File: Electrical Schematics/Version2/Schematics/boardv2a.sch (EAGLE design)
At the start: 622 parts, among them IC1 MCP41HVX1ST, IC2 ADUM4160BRW, IC3 SE555D, IC5 74LVC1G04DBV, IC6 74LVC1G04DBV, IC7 4030D, K1 G5V-2, K2 CP1SA-12V, Q1 IRLML2060TRPBFBSS123LT1G, Q10 IRLML2060TRPBFBSS123LT1G, Q11 IRLML2060TRPBFBSS123LT1G, Q12 IRLML2060TRPBFBSS123LT1G, Q13 IRLML2060TRPBFBSS123LT1G, Q17 IRLML2060TRPBFBSS123LT1G, Q18 MOSFET-PCHANNEL, Q19 IRLML2060TRPBFBSS123LT1G, Q2 IRLML2060TRPBFBSS123LT1G, Q3 IRLML2060TRPBFBSS123LT1G, Q4 MOSFET-PCHANNEL, Q5 MOSFET-PCHANNEL, Q6 IRLML2060TRPBFBSS123LT1G, Q7 ASFL1, Q8 IRLML2060TRPBFBSS123LT1G, Q9 IRLML2060TRPBFBSS123LT1G, U1 CP2130-GM, U10 SN65HVDA100-Q1_D_8, U11 ADUM3442CRWZ, U12 ADUM3442CRWZ, U13 ADUM3442CRWZ, U14 ADUM3442CRWZ, U15 ADUM3442CRWZ, U16 ADUM3442CRWZ, U17 ADUM3442CRWZ, U18 LM1085_KTT_3, U19 ADUM3442CRWZ, U2 TMS570LS0432_PZ_100, U20 ADUM3442CRWZ, U3 LM1085_KTT_3, U4 LM1085_KTT_3, U5 LM1084_KTT_3, U6 TPS3514_D_14, U7 LM1085_KTT_3, U9 ADUM3442CRWZ, X4 5566-4

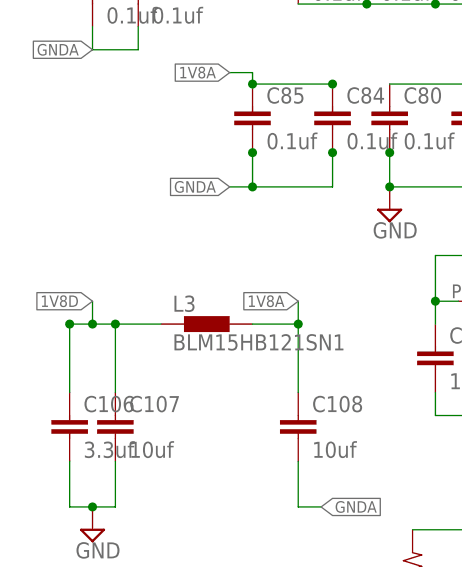
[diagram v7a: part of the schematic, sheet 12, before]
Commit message: routed lin ethernet and usb
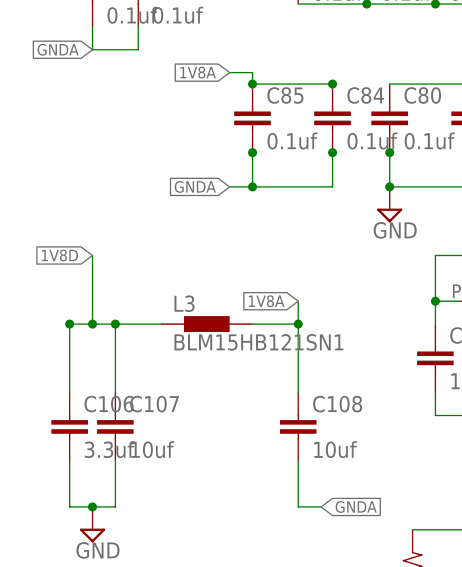
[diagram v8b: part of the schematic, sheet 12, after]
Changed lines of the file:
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@@
 <setting verticaltext="up"/>
 </settings>
-<grid distance="0.05" unitdist="inch" unit="inch" style="lines" multiple="1" display="no" altdistance="0.025" altunitdist="inch" altunit="inch"/>
+<grid distance="0.1" unitdist="inch" unit="inch" style="lines" multiple="1" display="no" altdistance="0.01" altunitdist="inch" altunit="inch"/>
 <layers>
-<layer number="1" name="Top" color="4" fill="1" visible="yes" active="no"/>
-<layer number="2" name="Route2" color="1" fill="3" visible="yes" active="no"/>
-<layer number="3" name="Route3" color="4" fill="3" visible="yes" active="no"/>
-<layer number="4" name="Route4" color="1" fill="4" visible="yes" active="no"/>
-<layer number="5" name="Route5" color="4" fill="4" visible="yes" active="no"/>
-<layer number="6" name="Route6" color="1" fill="8" visible="yes" active="no"/>
-<layer number="7" name="Route7" color="4" fill="8" visible="yes" active="no"/>
-<layer number="8" name="Route8" color="1" fill="2" visible="yes" active="no"/>
-<layer number="9" name="Route9" color="4" fill="2" visible="yes" active="no"/>
-<layer number="10" name="Route10" color="1" fill="7" visible="yes" active="no"/>
-<layer number="11" name="Route11" color="4" fill="7" visible="yes" active="no"/>
-<layer number="12" name="Route12" color="1" fill="5" visible="yes" active="no"/>
-<layer number="13" name="Route13" color="4" fill="5" visible="yes" active="no"/>
-<layer number="14" name="Route14" color="1" fill="6" visible="yes" active="no"/>
-<layer number="15" name="Route15" color="4" fill="6" visible="yes" active="no"/>
-<layer number="16" name="Bottom" color="1" fill="1" visible="yes" active="no"/>
-<layer number="17" name="Pads" color="2" fill="1" visible="yes" active="no"/>
-<layer number="18" name="Vias" color="2" fill="1" visible="yes" active="no"/>
-<layer number="19" name="Unrouted" color="6" fill="1" visible="yes" active="no"/>
-<layer number="20" name="Dimension" color="15" fill="1" visible="yes" active="no"/>
-<layer number="21" name="tPlace" color="7" fill="1" visible="yes" active="no"/>
-<layer number="22" name="bPlace" color="7" fill="1" visible="yes" active="no"/>
-<layer number="23" name="tOrigins" color="15" fill="1" visible="yes" active="no"/>
-<layer number="24" name="bOrigins" color="15" fill="1" visible="yes" active="no"/>
-<layer number="25" name="tNames" color="7" fill="1" visible="yes" active="no"/>
-<layer number="26" name="bNames" color="7" fill="1" visible="yes" active="no"/>
-<layer number="27" name="tValues" color="7" fill="1" visible="yes" active="no"/>
-<layer number="28" name="bValues" color="7" fill="1" visible="yes" active="no"/>
+<layer number="1" name="Top" color="4" fill="1" visible="no" active="no"/>
+<layer number="2" name="Route2" color="1" fill="3" visible="no" active="no"/>
+<layer number="3" name="Route3" color="4" fill="3" visible="no" active="no"/>
+<layer number="4" name="Route4" color="1" fill="4" visible="no" active="no"/>
+<layer number="5" name="Route5" color="4" fill="4" visible="no" active="no"/>
+<layer number="6" name="Route6" color="1" fill="8" visible="no" active="no"/>
+<layer number="7" name="Route7" color="4" fill="8" visible="no" active="no"/>
+<layer number="8" name="Route8" color="1" fill="2" visible="no" active="no"/>
+<layer number="9" name="Route9" color="4" fill="2" visible="no" active="no"/>
+<layer number="10" name="Route10" color="1" fill="7" visible="no" active="no"/>
+<layer number="11" name="Route11" color="4" fill="7" visible="no" active="no"/>
+<layer number="12" name="Route12" color="1" fill="5" visible="no" active="no"/>
+<layer number="13" name="Route13" color="4" fill="5" visible="no" active="no"/>
+<layer number="14" name="Route14" color="1" fill="6" visible="no" active="no"/>
+<layer number="15" name="Route15" color="4" fill="6" visible="no" active="no"/>
+<layer number="16" name="Bottom" color="1" fill="1" visible="no" active="no"/>
+<layer number="17" name="Pads" color="2" fill="1" visible="no" active="no"/>
+<layer number="18" name="Vias" color="2" fill="1" visible="no" active="no"/>
+<layer number="19" name="Unrouted" color="6" fill="1" visible="no" active="no"/>
+<layer number="20" name="Dimension" color="15" fill="1" visible="no" active="no"/>
+<layer number="21" name="tPlace" color="7" fill="1" visible="no" active="no"/>
+<layer number="22" name="bPlace" color="7" fill="1" visible="no" active="no"/>
+<layer number="23" name="tOrigins" color="15" fill="1" visible="no" active="no"/>
+<layer number="24" name="bOrigins" color="15" fill="1" visible="no" active="no"/>
+<layer number="25" name="tNames" color="7" fill="1" visible="no" active="no"/>
+<layer number="26" name="bNames" color="7" fill="1" visible="no" active="no"/>
+<layer number="27" name="tValues" color="7" fill="1" visible="no" active="no"/>
+<layer number="28" name="bValues" color="7" fill="1" visible="no" active="no"/>
 <layer number="29" name="tStop" color="7" fill="3" visible="no" active="no"/>
 <layer number="30" name="bStop" color="7" fill="6" visible="no" active="no"/>
@@
 <layer number="35" name="tGlue" color="7" fill="4" visible="no" active="no"/>
 <layer number="36" name="bGlue" color="7" fill="5" visible="no" active="no"/>
-<layer number="37" name="tTest" color="7" fill="1" visible="yes" active="no"/>
-<layer number="38" name="bTest" color="7" fill="1" visible="yes" active="no"/>
+<layer number="37" name="tTest" color="7" fill="1" visible="no" active="no"/>
+<layer number="38" name="bTest" color="7" fill="1" visible="no" active="no"/>
 <layer number="39" name="tKeepout" color="4" fill="11" visible="no" active="no"/>
 <layer number="40" name="bKeepout" color="1" fill="11" visible="no" active="no"/>
@@
 <layer number="44" name="Drills" color="7" fill="1" visible="no" active="no"/>
 <layer number="45" name="Holes" color="7" fill="1" visible="no" active="no"/>
-<layer number="46" name="Milling" color="3" fill="1" visible="yes" active="no"/>
-<layer number="47" name="Measures" color="7" fill="1" visible="yes" active="no"/>
-<layer number="48" name="Document" color="7" fill="1" visible="yes" active="no"/>
-<layer number="49" name="Reference" color="7" fill="1" visible="yes" active="no"/>
-<layer number="50" name="dxf" color="7" fill="1" visible="yes" active="no"/>
-<layer number="51" name="tDocu" color="7" fill="1" visible="yes" active="no"/>
-<layer number="52" name="bDocu" color="7" fill="1" visible="yes" active="no"/>
-<layer number="53" name="tGND_GNDA" color="7" fill="9" visible="yes" active="no"/>
-<layer number="54" name="bGND_GNDA" color="1" fill="9" visible="yes" active="no"/>
-<layer number="56" name="wert" color="7" fill="1" visible="yes" active="no"/>
-<layer number="57" name="tCAD" color="7" fill="1" visible="yes" active="no"/>
+<layer number="46" name="Milling" color="3" fill="1" visible="no" active="no"/>
+<layer number="47" name="Measures" color="7" fill="1" visible="no" active="no"/>
+<layer number="48" name="Document" color="7" fill="1" visible="no" active="no"/>
+<layer number="49" name="Reference" color="7" fill="1" visible="no" active="no"/>
+<layer number="50" name="dxf" color="7" fill="1" visible="no" active="no"/>
+<layer number="51" name="tDocu" color="7" fill="1" visible="no" active="no"/>
+<layer number="52" name="bDocu" color="7" fill="1" visible="no" active="no"/>
+<layer number="53" name="tGND_GNDA" color="7" fill="9" visible="no" active="no"/>
+<layer number="54" name="bGND_GNDA" color="1" fill="9" visible="no" active="no"/>
+<layer number="56" name="wert" color="7" fill="1" visible="no" active="no"/>
+<layer number="57" name="tCAD" color="7" fill="1" visible="no" active="no"/>
 <layer number="90" name="Modules" color="5" fill="1" visible="yes" active="yes"/>
 <layer number="91" name="Nets" color="2" fill="1" visible="yes" active="yes"/>
@@
 <wire x1="-38.1" y1="63.5" x2="-33.02" y2="63.5" width="0.1524" layer="91"/>
 <pinref part="L3" gate="G$1" pin="1"/>
-<wire x1="-40.64" y1="63.5" x2="-40.64" y2="66.04" width="0.1524" layer="91"/>
-<label x="-40.64" y="66.04" size="1.27" layer="95" rot="R180" xref="yes"/>
+<wire x1="-40.64" y1="63.5" x2="-40.64" y2="71.12" width="0.1524" layer="91"/>
+<label x="-40.64" y="71.12" size="1.27" layer="95" rot="R180" xref="yes"/>
 <junction x="-43.18" y="63.5"/>
 <junction x="-38.1" y="63.5"/>
